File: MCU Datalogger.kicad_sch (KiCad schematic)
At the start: 25 parts, among them U1 24LC1025, U2 24LC1025, U3 DS1337S_, U4 ATMEGA328P-AU, Y1 Crystal, Y2 Crystal

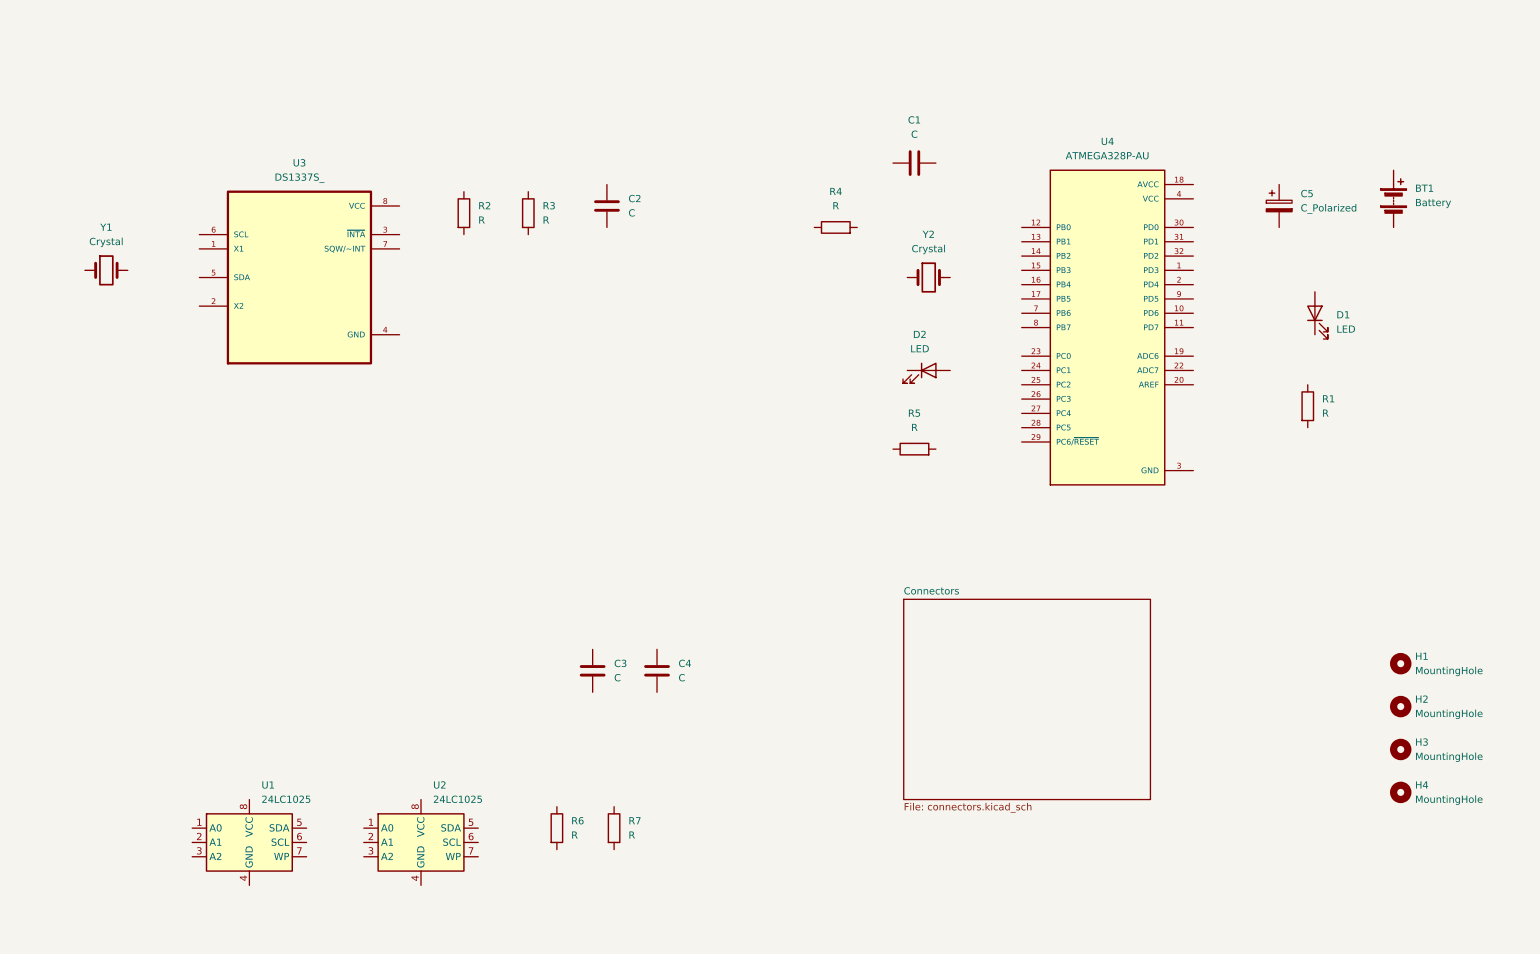
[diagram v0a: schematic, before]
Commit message: Added component values
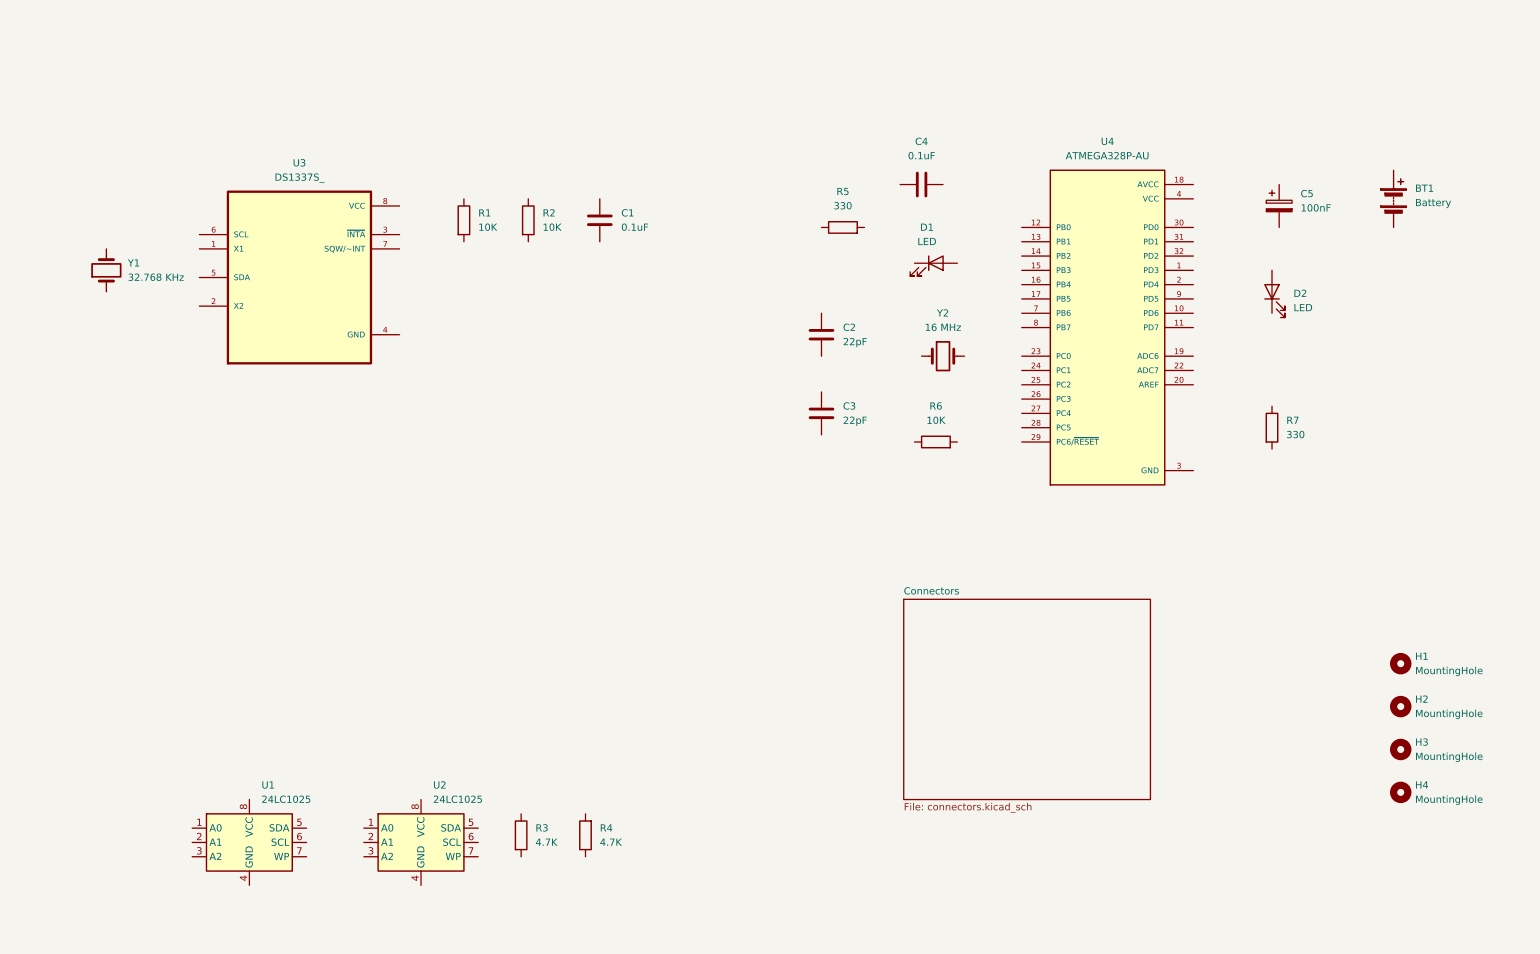
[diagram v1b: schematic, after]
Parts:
- C1, C4: value C -> 0.1uF
- C2, C3: value C -> 22pF
- C5: value C_Polarized -> 100nF
- R1, R2, R6: value R -> 10K
- R3, R4: value R -> 4.7K
- R5, R7: value R -> 330
- Y1: value Crystal -> 32.768 KHz
- Y2: value Crystal -> 16 MHz
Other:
- moved on the sheet: C1, C2, C3, C4, D1, D2, R1, R2, R3, R4, R5, R6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

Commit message: Completed symbol-footprint associations
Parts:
- BT1: footprint (none) -> Connector_PinHeader_2.54mm:PinHeader_1x02_P2.54mm_Vertical
- C1, C2, C3, C4, C5: footprint (none) -> Capacitor_SMD:C_0805_2012Metric
- D1, D2: footprint (none) -> LED_SMD:LED_0805_2012Metric
- H1, H2, H3, H4: footprint (none) -> MountingHole:MountingHole_2.1mm
- R1, R2, R3, R4, R5, R6, R7: footprint (none) -> Resistor_SMD:R_0805_2012Metric
- U1, U2: footprint (none) -> Package_SO:SOIC-8_5.3x5.3mm_P1.27mm
- Y1, Y2: footprint (none) -> Crystal:Crystal_SMD_5032-2Pin_5.0x3.2mm_HandSoldering
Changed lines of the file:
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@@
 			)
 		)
-		(property "Footprint" ""
+		(property "Footprint" "LED_SMD:LED_0805_2012Metric"
 			(at 177.8 60.96 0)
 			(hide yes)
@@
 			)
 		)
-		(property "Footprint" ""
+		(property "Footprint" "Capacitor_SMD:C_0805_2012Metric"
 			(at 158.4452 91.44 0)
 			(hide yes)
@@
 			)
 		)
-		(property "Footprint" ""
+		(property "Footprint" "Resistor_SMD:R_0805_2012Metric"
 			(at 102.362 162.56 90)
 			(hide yes)
@@
 			)
 		)
-		(property "Footprint" ""
+		(property "Footprint" "MountingHole:MountingHole_2.1mm"
 			(at 260.35 139.7 0)
 			(hide yes)
@@
 			)
 		)
-		(property "Footprint" ""
+		(property "Footprint" "Resistor_SMD:R_0805_2012Metric"
 			(at 177.8 94.488 90)
 			(hide yes)
@@
 			)
 		)
-		(property "Footprint" ""
+		(property "Footprint" "Resistor_SMD:R_0805_2012Metric"
 			(at 92.202 53.34 90)
 			(hide yes)
@@
 			)
 		)
-		(property "Footprint" ""
+		(property "Footprint" "Capacitor_SMD:C_0805_2012Metric"
 			(at 239.7252 54.61 0)
 			(hide yes)
@@
 			)
 		)
-		(property "Footprint" ""
+		(property "Footprint" "Capacitor_SMD:C_0805_2012Metric"
 			(at 117.1448 49.53 0)
 			(hide yes)
@@
 			)
 		)
-		(property "Footprint" ""
+		(property "Footprint" "Package_SO:SOIC-8_5.3x5.3mm_P1.27mm"
 			(at 55.88 163.83 0)
 			(hide yes)
@@
 			)
 		)
-		(property "Footprint" ""
+		(property "Footprint" "LED_SMD:LED_0805_2012Metric"
 			(at 237.49 66.04 0)
 			(hide yes)
@@
 			)
 		)
-		(property "Footprint" ""
+		(property "Footprint" "Crystal:Crystal_SMD_5032-2Pin_5.0x3.2mm_HandSoldering"
 			(at 30.48 62.23 0)
 			(hide yes)
@@
 			)
 		)
-		(property "Footprint" ""
+		(property "Footprint" "Connector_PinHeader_2.54mm:PinHeader_1x02_P2.54mm_Vertical"
 			(at 259.08 48.006 90)
 			(hide yes)
@@
 			)
 		)
-		(property "Footprint" ""
+		(property "Footprint" "MountingHole:MountingHole_2.1mm"
 			(at 260.35 147.32 0)
 			(hide yes)
@@
 			)
 		)
-		(property "Footprint" ""
+		(property "Footprint" "MountingHole:MountingHole_2.1mm"
 			(at 260.35 154.94 0)
 			(hide yes)
@@
 			)
 		)
-		(property "Footprint" ""
+		(property "Footprint" "Package_SO:SOIC-8_5.3x5.3mm_P1.27mm"
 			(at 86.36 163.83 0)
 			(hide yes)
@@
 			)
 		)
-		(property "Footprint" ""
+		(property "Footprint" "Capacitor_SMD:C_0805_2012Metric"
 			(at 156.5148 69.85 0)
 			(hide yes)
@@
 			)
 		)
-		(property "Footprint" ""
+		(property "Footprint" "Resistor_SMD:R_0805_2012Metric"
 			(at 117.348 162.56 90)
 			(hide yes)
@@
 			)
 		)
-		(property "Footprint" ""
+		(property "Footprint" "Resistor_SMD:R_0805_2012Metric"
 			(at 103.632 53.34 90)
 			(hide yes)
@@
 			)
 		)
-		(property "Footprint" ""
+		(property "Footprint" "Resistor_SMD:R_0805_2012Metric"
 			(at 235.712 90.17 90)
 			(hide yes)
@@
 			)
 		)
-		(property "Footprint" ""
+		(property "Footprint" "Resistor_SMD:R_0805_2012Metric"
 			(at 161.29 56.388 90)
 			(hide yes)
@@
 			)
 		)
-		(property "Footprint" ""
+		(property "Footprint" "Crystal:Crystal_SMD_5032-2Pin_5.0x3.2mm_HandSoldering"
 			(at 179.07 77.47 0)
 			(hide yes)
@@
 			)
 		)
-		(property "Footprint" ""
+		(property "Footprint" "Capacitor_SMD:C_0805_2012Metric"
 			(at 179.07 46.0248 0)
 			(hide yes)
@@
 			)
 		)
-		(property "Footprint" ""
+		(property "Footprint" "MountingHole:MountingHole_2.1mm"
 			(at 260.35 132.08 0)
 			(hide yes)

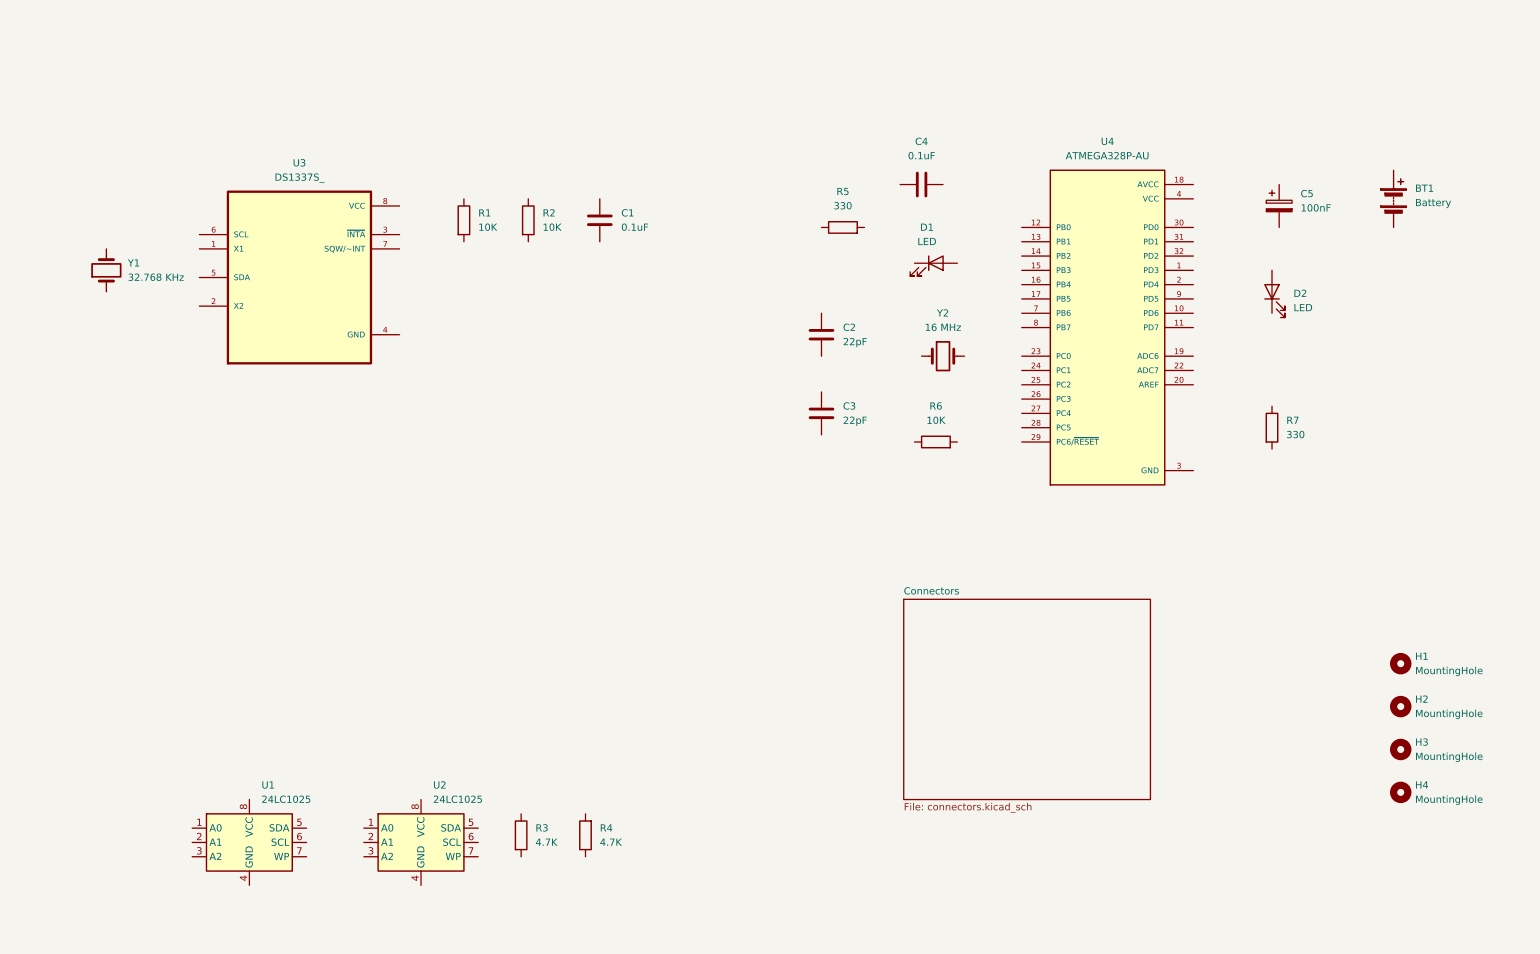
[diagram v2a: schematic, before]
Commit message: Completed wiring of main sheet
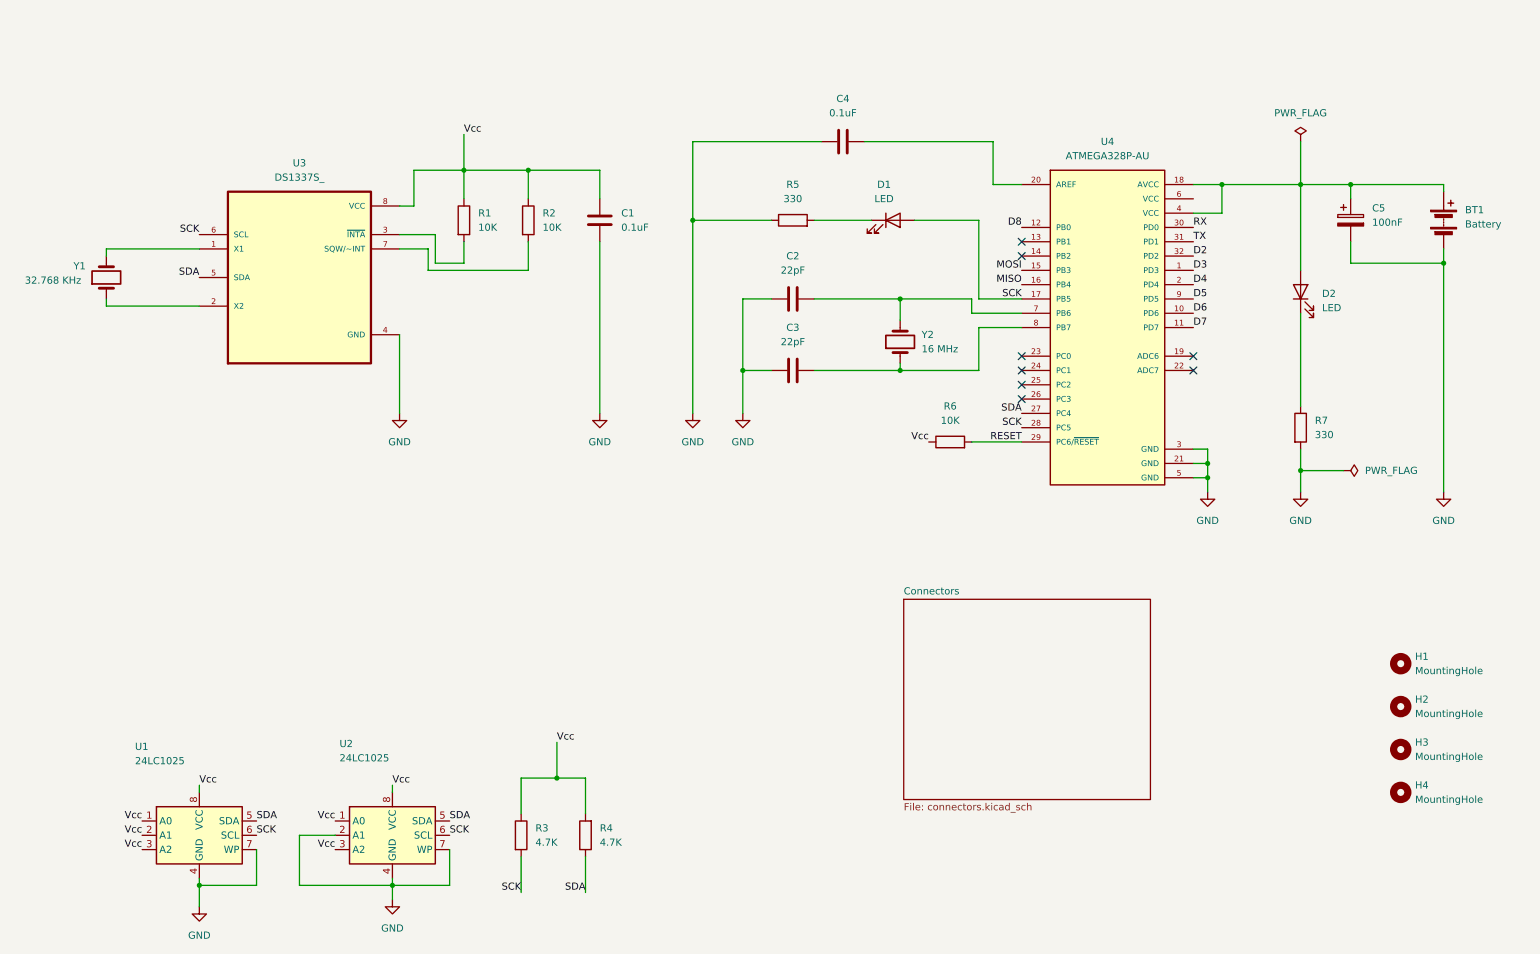
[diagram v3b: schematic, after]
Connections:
- net GND: now also BT1.2 (-), C1.1, C2.2, C3.1, C4.1, C5.2, R5.1, R7.2, U1.4 (GND), U1.7 (WP), U2.2 (A1), U2.4 (GND), U2.7 (WP), U3.4 (GND)
- net at D1.1 (K): now also R5.2
- net SCK: now reaches D1.2 (A)
- net SCK: now also R3.2, U1.6 (SCL), U2.6 (SCL), U3.6 (SCL), U4.17 (PB5), U4.28 (PC5)
- net at C3.2: now also U4.8 (PB7), Y2.1
- net Vcc: now reaches R3.1
- net Vcc: now also C1.2, R1.1, R2.1, R4.2, R6.1, U1.1 (A0), U1.2 (A1), U1.3 (A2), U1.8 (VCC), U2.1 (A0), U2.3 (A2), U2.8 (VCC), U3.8 (VCC)
- net RESET: now reaches R6.2
- net RESET: now also U4.29 (PC6/~{RESET})
- net at R1.2: now also U3.3 (~{INTA})
- net at C5.1: now also BT1.1 (+), D2.2 (A), U4.18 (AVCC), U4.4 (VCC)
- net at U3.1 (X1): now also Y1.2
- net at U3.2 (X2): now also Y1.1
- net SDA: now reaches U3.5 (SDA)
- net SDA: now also R4.1, U1.5 (SDA), U2.5 (SDA), U4.27 (PC4)
- net at U3.7 (SQW/~INT): now also R2.2
- net at D2.1 (K): now also R7.1
- net D3: now reaches U4.1 (PD3)
- net D6: now reaches U4.10 (PD6)
- net D7: now reaches U4.11 (PD7)
- net D8: now reaches U4.12 (PB0)
- net MOSI: now reaches U4.15 (PB3)
- net MISO: now reaches U4.16 (PB4)
- net D4: now reaches U4.2 (PD4)
- net at U4.20 (AREF): now also C4.2
- net RX: now reaches U4.30 (PD0)
- net TX: now reaches U4.31 (PD1)
- net D2: now reaches U4.32 (PD2)
- net at U4.7 (PB6): now also C2.1, Y2.2
- net D5: now reaches U4.9 (PD5)
- net VCC: no longer names the net of U4.6 (VCC)
- net VCC: no longer U4.4 (VCC)
- no-connect marks 0 -> 8
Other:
- moved on the sheet: BT1, C2, C3, C4, C5, D1, D2, R5, R6, R7, U1, U2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

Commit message: Completed wiring of the second sheet
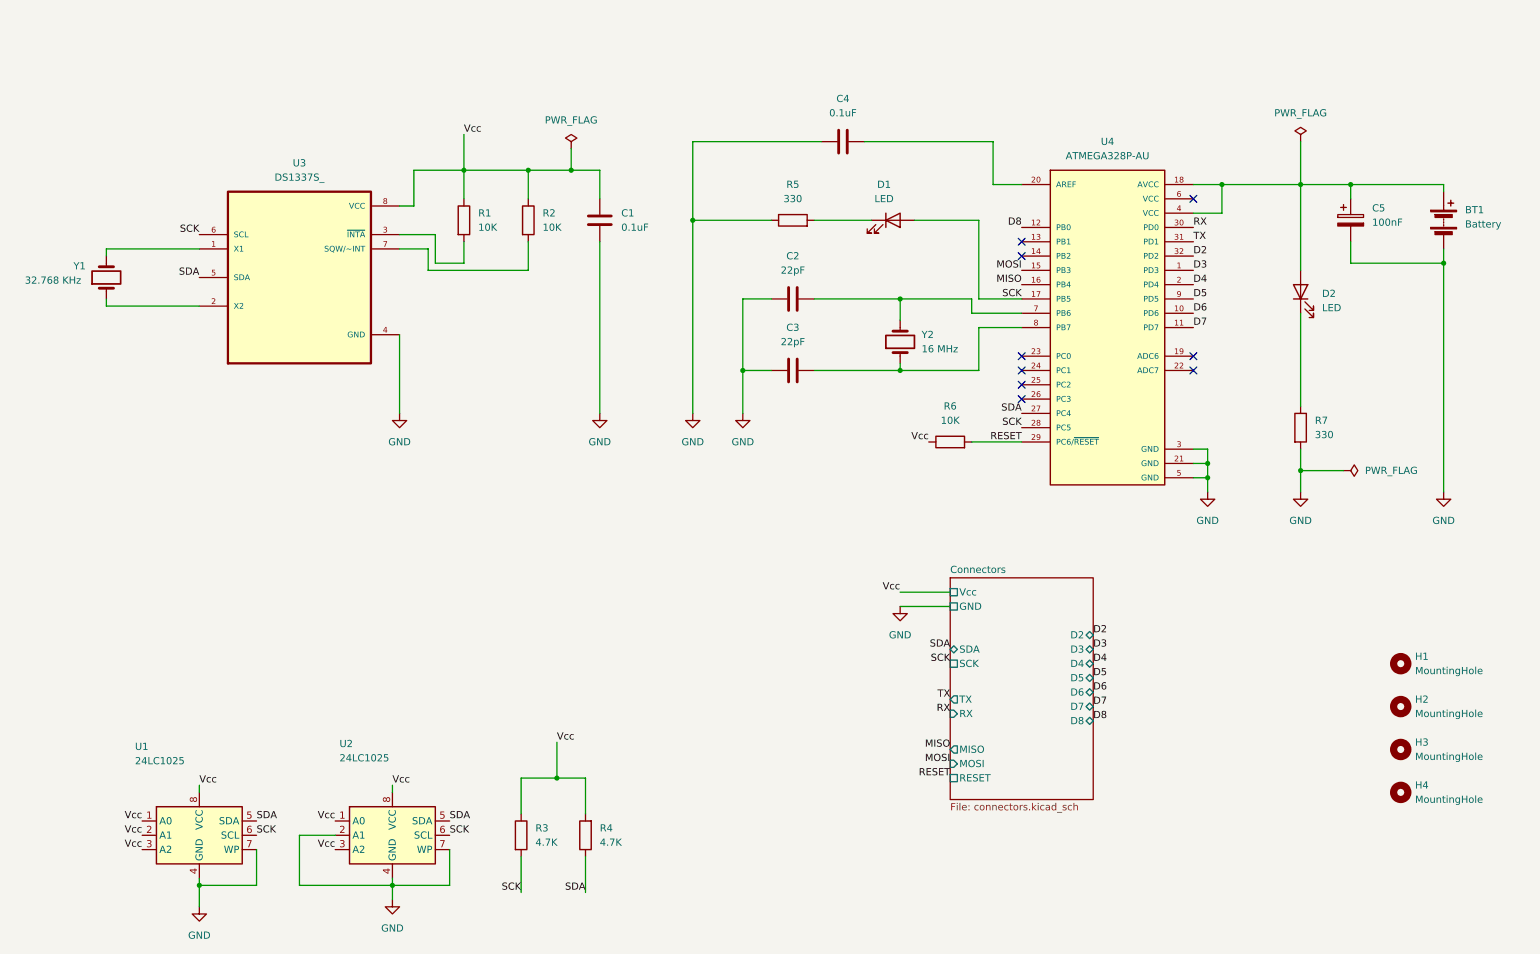
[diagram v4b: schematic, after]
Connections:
- no-connect marks 8 -> 9
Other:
- sheet Connectors ports: added D2, D3, D4, D5, D6, D7, D8, GND, MISO, MOSI, RESET, RX, SCK, SDA, TX, Vcc; removed none

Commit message: Completed comments
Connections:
- net Vcc renamed VCC
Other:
- sheet Connectors ports: added VCC; removed Vcc
- note added: "EEPROM"
- note added: "MCU"
- note added: "Mounting"
- note added: "Real-time Clock"
- moved on the sheet: BT1, C2, C3, C4, C5, D1, D2, H1, H2, H3, H4, R3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

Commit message: Partial routing in front and back layers
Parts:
- renumbered U3 to U2, U2 to U3
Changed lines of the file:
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@@
 		(dnp no)
 		(fields_autoplaced yes)
-		(property "Reference" "U3"
+		(property "Reference" "U2"
 			(at 64.77 43.18 0)
 			(show_name no)
@@
 			(project "MCU Datalogger"
 				(path "/b6931e11-5ca4-40d2-8041-2a917f2b0362"
-					(reference "U3")
+					(reference "U2")
 					(unit 1)
 				)
@@
 		(in_pos_files yes)
 		(dnp no)
-		(property "Reference" "U2"
+		(property "Reference" "U3"
 			(at 65.532 122.174 0)
 			(show_name no)
@@
 			(project "MCU Datalogger"
 				(path "/b6931e11-5ca4-40d2-8041-2a917f2b0362"
-					(reference "U2")
+					(reference "U3")
 					(unit 1)
 				)
